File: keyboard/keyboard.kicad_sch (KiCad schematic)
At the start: 16 parts, among them J1 Conn_01x22, J10 Conn_01x01, J11 Conn_01x01, J12 Conn_01x01, J13 Conn_01x01, J14 Conn_01x01, J15 Conn_01x01, J16 Conn_01x01, J2 Conn_01x22, J3 Conn_01x01, J4 Conn_01x01, J5 Conn_01x01, J6 Conn_01x01, J7 Conn_01x01, J8 Conn_01x01, J9 Conn_01x01

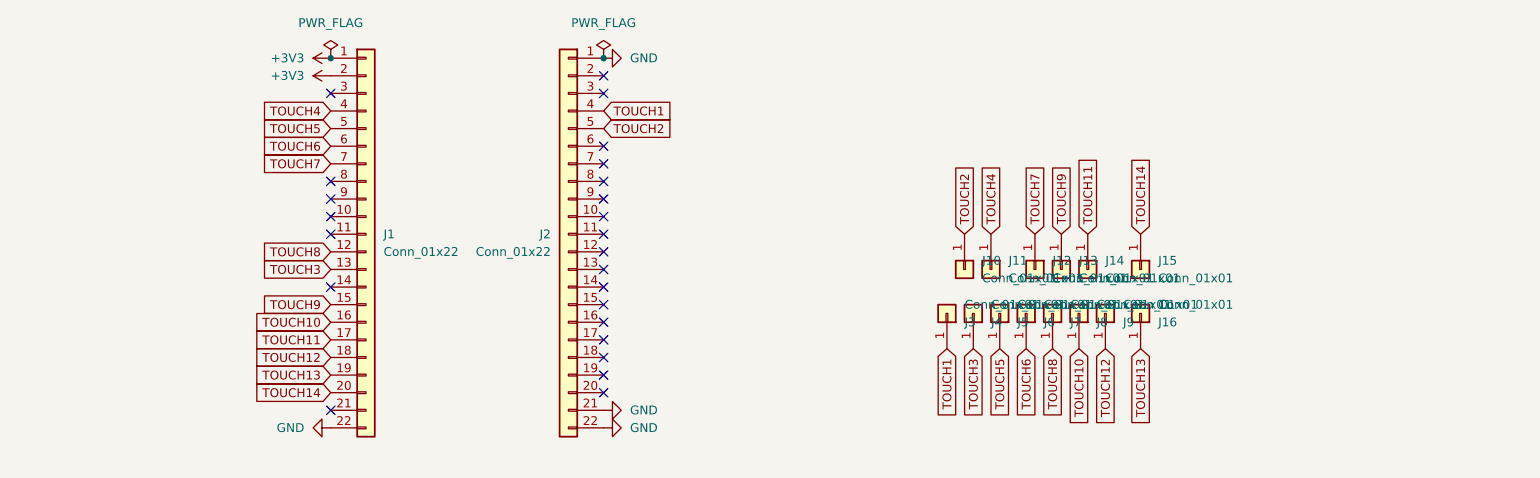
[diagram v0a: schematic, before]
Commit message: Add symbol and footprints libraries to keyboard
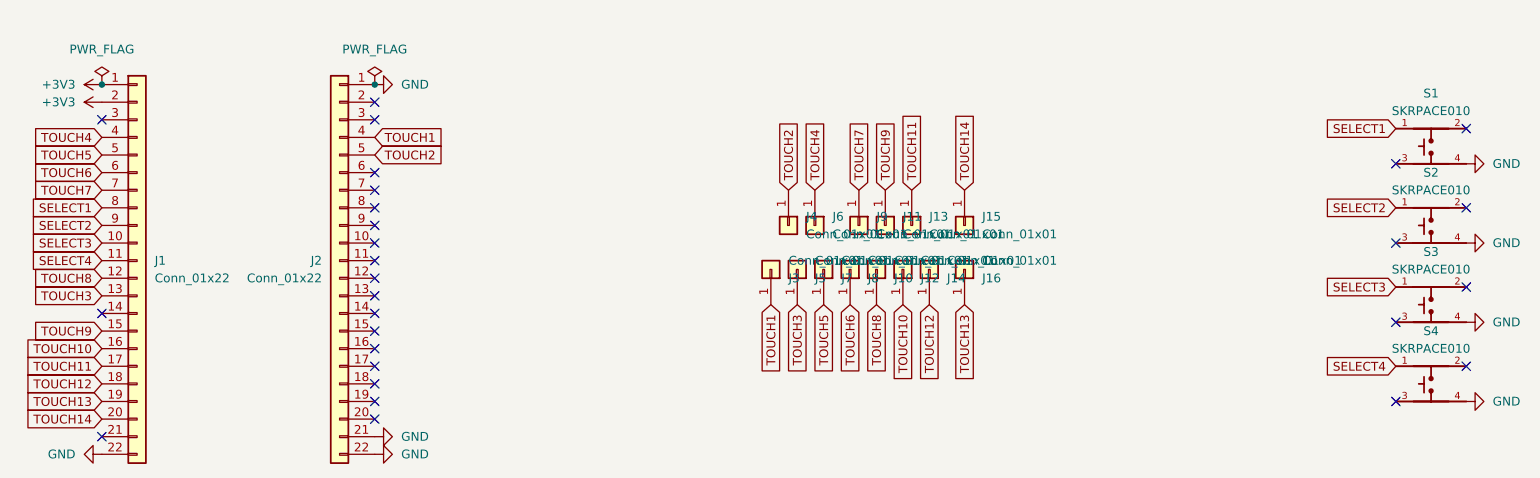
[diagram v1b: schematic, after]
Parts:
- added S1, S2, S3, S4: SKRPACE010, SKRPACE010:SKRPACE010, symbol SKRPACE010:SKRPACE010
- J10, J11, J12, J13, J14, J15, J16, J3, J4, J5, J6, J7, J8, J9: footprint SparkFun-Switch:Pad-CapacitiveTouch -> Pad-CapacitiveTouch:Pad-CapacitiveTouch
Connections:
- net GND: now also S1.4, S2.4, S3.4, S4.4
- net TOUCH10: now also J12.1 (Pin_1); no longer J8.1 (Pin_1)
- net TOUCH11: now also J13.1 (Pin_1); no longer J14.1 (Pin_1)
- net TOUCH12: now also J14.1 (Pin_1); no longer J9.1 (Pin_1)
- net TOUCH2: now also J4.1 (Pin_1); no longer J10.1 (Pin_1)
- net TOUCH3: now also J5.1 (Pin_1); no longer J4.1 (Pin_1)
- net TOUCH4: now also J6.1 (Pin_1); no longer J11.1 (Pin_1)
- net TOUCH5: now also J7.1 (Pin_1); no longer J5.1 (Pin_1)
- net TOUCH6: now also J8.1 (Pin_1); no longer J6.1 (Pin_1)
- net TOUCH7: now also J9.1 (Pin_1); no longer J12.1 (Pin_1)
- net TOUCH8: now also J10.1 (Pin_1); no longer J7.1 (Pin_1)
- net TOUCH9: now also J11.1 (Pin_1); no longer J13.1 (Pin_1)
- net SELECT3: now reaches J1.10 (Pin_10)
- net SELECT3: now also S3.1
- net SELECT4: now reaches J1.11 (Pin_11)
- net SELECT4: now also S4.1
- net SELECT1: now reaches J1.8 (Pin_8)
- net SELECT1: now also S1.1
- net SELECT2: now reaches J1.9 (Pin_9)
- net SELECT2: now also S2.1
- no-connect marks 24 -> 28

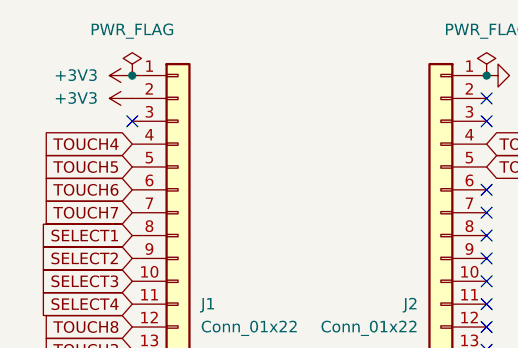
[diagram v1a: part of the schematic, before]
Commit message: Delete +3V3 from 4 dev boards
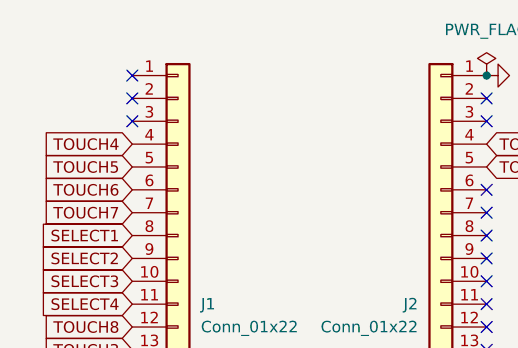
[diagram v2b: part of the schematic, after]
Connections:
- net +3V3: no longer names the net of J1.1 (Pin_1)
- net +3V3: no longer J1.2 (Pin_2)
- no-connect marks 28 -> 30
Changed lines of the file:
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@@
 	(paper "A4")
-	(junction
-		(at 53.34 64.77)
-		(diameter 0)
-		(color 0 0 0 0)
-	)
 	(junction
 		(at 92.71 64.77)
@@
 	)
 	(no_connect
+		(at 53.34 67.31)
+	)
+	(no_connect
 		(at 92.71 90.17)
 	)
@@
 	(no_connect
 		(at 92.71 105.41)
+	)
+	(no_connect
+		(at 53.34 64.77)
 	)
 	(no_connect
@@
 				(path "/e77fdaa9-127d-430b-b7ed-66bcd534fe2d"
 					(reference "S1")
-					(unit 1)
-				)
-			)
-		)
-	)
-	(symbol
-		(lib_id "power:+3V3")
-		(at 53.34 67.31 90)
-		(unit 1)
-		(exclude_from_sim no)
-		(in_bom yes)
-		(on_board yes)
-		(dnp no)
-		(fields_autoplaced yes)
-		(property "Reference" "#PWR02"
-			(at 57.15 67.31 0)
-			(effects
-				(font
-					(size 1.27 1.27)
-				)
-				(hide yes)
-			)
-		)
-		(property "Value" "+3V3"
-			(at 49.53 67.3099 90)
-			(effects
-				(font
-					(size 1.27 1.27)
-				)
-				(justify left)
-			)
-		)
-		(property "Footprint" ""
-			(at 53.34 67.31 0)
-			(effects
-				(font
-					(size 1.27 1.27)
-				)
-				(hide yes)
-			)
-		)
-		(property "Datasheet" ""
-			(at 53.34 67.31 0)
-			(effects
-				(font
-					(size 1.27 1.27)
-				)
-				(hide yes)
-			)
-		)
-		(property "Description" "Power symbol creates a global label with name \"+3V3\""
-			(at 53.34 67.31 0)
-			(effects
-				(font
-					(size 1.27 1.27)
-				)
-				(hide yes)
-			)
-		)
-		(pin "1"
-		)
-		(instances
-			(project "keyboard"
-				(path "/e77fdaa9-127d-430b-b7ed-66bcd534fe2d"
-					(reference "#PWR02")
 					(unit 1)
 				)
@@
 	)
 	(symbol
-		(lib_id "power:+3V3")
-		(at 53.34 64.77 90)
-		(unit 1)
-		(exclude_from_sim no)
-		(in_bom yes)
-		(on_board yes)
-		(dnp no)
-		(fields_autoplaced yes)
-		(property "Reference" "#PWR01"
-			(at 57.15 64.77 0)
-			(effects
-				(font
-					(size 1.27 1.27)
-				)
-				(hide yes)
-			)
-		)
-		(property "Value" "+3V3"
-			(at 49.53 64.7699 90)
-			(effects
-				(font
-					(size 1.27 1.27)
-				)
-				(justify left)
-			)
-		)
-		(property "Footprint" ""
-			(at 53.34 64.77 0)
-			(effects
-				(font
-					(size 1.27 1.27)
-				)
-				(hide yes)
-			)
-		)
-		(property "Datasheet" ""
-			(at 53.34 64.77 0)
-			(effects
-				(font
-					(size 1.27 1.27)
-				)
-				(hide yes)
-			)
-		)
-		(property "Description" "Power symbol creates a global label with name \"+3V3\""
-			(at 53.34 64.77 0)
-			(effects
-				(font
-					(size 1.27 1.27)
-				)
-				(hide yes)
-			)
-		)
-		(pin "1"
-		)
-		(instances
-			(project "keyboard"
-				(path "/e77fdaa9-127d-430b-b7ed-66bcd534fe2d"
-					(reference "#PWR01")
-					(unit 1)
-				)
-			)
-		)
-	)
-	(symbol
 		(lib_id "power:GND")
 		(at 92.71 118.11 90)
@@
 					(unit 1)
 				)
-			)
-		)
-	)
-	(symbol
-		(lib_id "power:PWR_FLAG")
-		(at 53.34 64.77 0)
-		(unit 1)
-		(exclude_from_sim no)
-		(in_bom yes)
-		(on_board yes)
-		(dnp no)
-		(fields_autoplaced yes)
-		(property "Reference" "#FLG01"
-			(at 53.34 62.865 0)
-			(effects
-				(font
-					(size 1.27 1.27)
-				)
-				(hide yes)
-			)
-		)
-		(property "Value" "PWR_FLAG"
-			(at 53.34 59.69 0)
-			(effects
-				(font
-					(size 1.27 1.27)
-				)
-			)
-		)
-		(property "Footprint" ""
-			(at 53.34 64.77 0)
-			(effects
-				(font
-					(size 1.27 1.27)
-				)
-				(hide yes)
-			)
-		)
-		(property "Datasheet" "~"
-			(at 53.34 64.77 0)
-			(effects
-				(font
-					(size 1.27 1.27)
-				)
-				(hide yes)
-			)
-		)
-		(property "Description" "Special symbol for telling ERC where power comes from"
-			(at 53.34 64.77 0)
-			(effects
-				(font
-					(size 1.27 1.27)
-				)
-				(hide yes)
-			)
-		)
-		(pin "1"
-		)
-		(instances
-			(project "keyboard"
-				(path "/e77fdaa9-127d-430b-b7ed-66bcd534fe2d"
-					(reference "#FLG01")
-					(unit 1)
-				)
